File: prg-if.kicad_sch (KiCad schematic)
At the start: 30 parts, among them J201 PRG_USB, J202 MCU_RST, J203 MCU_BOOT0, J204 FT_TXD, J205 FT_RXD, J206 CONN_JTAG, Q201 MMBT3906, U201 FT2232HL, Y201 12MHz

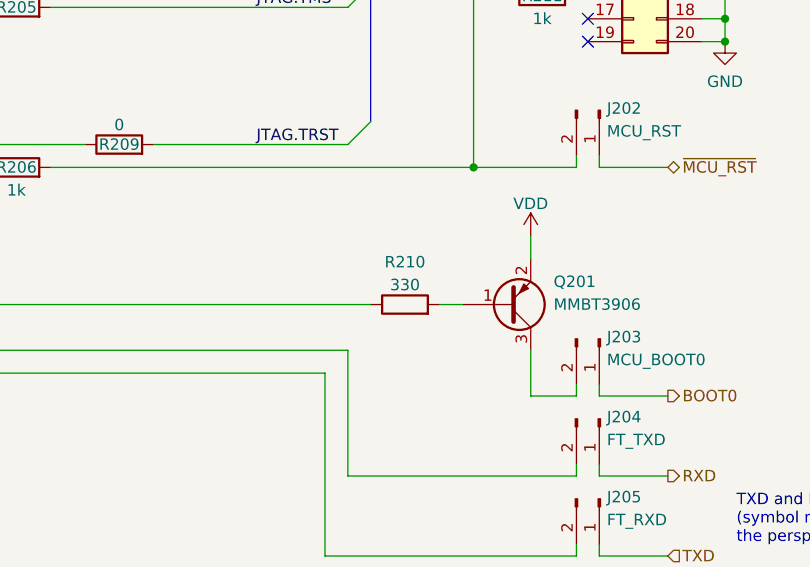
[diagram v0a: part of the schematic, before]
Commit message: Fix base resistor value
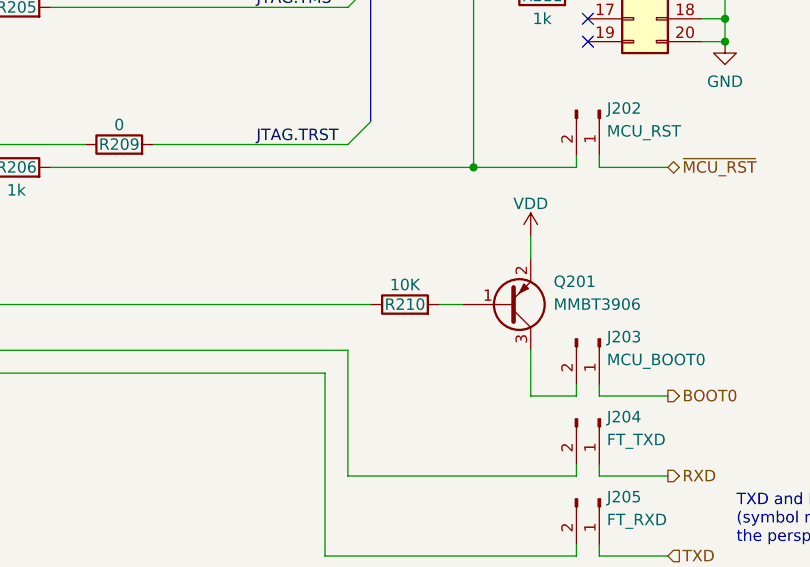
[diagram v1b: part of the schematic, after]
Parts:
- R210: value 330 -> 10K
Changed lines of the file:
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@@
   )
   (symbol (lib_id "Device:R") (at 214.63 106.68 90) (unit 1)
-    (in_bom yes) (on_board yes) (fields_autoplaced)
-    (property "Reference" "R210" (id 0) (at 214.63 101.9642 90))
-    (property "Value" "330" (id 1) (at 214.63 104.5011 90))
+    (in_bom yes) (on_board yes)
+    (property "Reference" "R210" (id 0) (at 214.63 106.68 90))
+    (property "Value" "10K" (id 1) (at 214.63 104.5011 90))
     (property "Footprint" "Resistor_SMD:R_0603_1608Metric_Pad0.98x0.95mm_HandSolder" (id 2) (at 214.63 108.458 90)
       (effects (font (size 1.27 1.27)) hide)

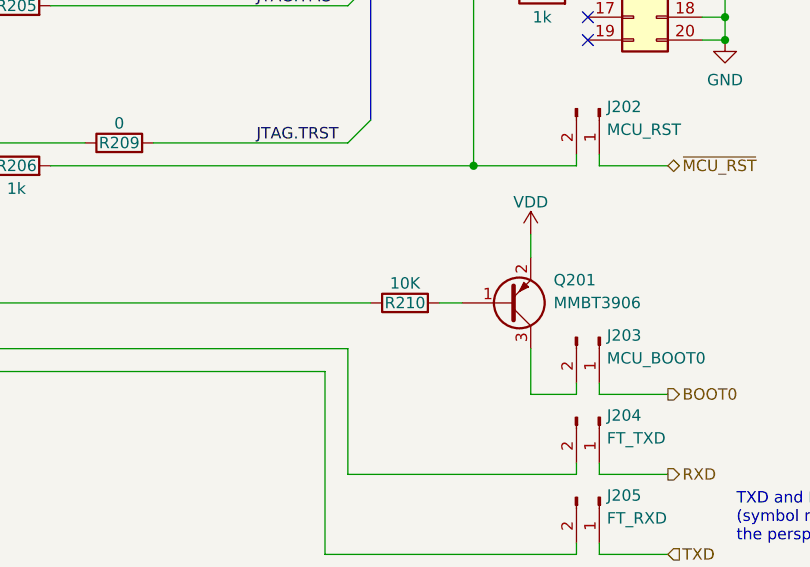
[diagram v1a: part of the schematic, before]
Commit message: Fully update PCB and schematic after BOM consolidation
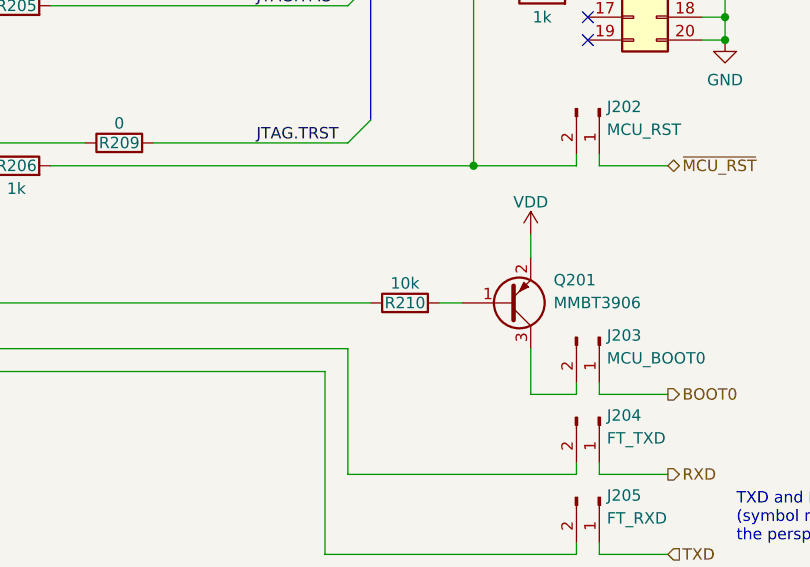
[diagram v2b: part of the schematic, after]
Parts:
- C201, C202: Part (none) -> 187-CL10C120JB81PNC
- C203, C206: Part 647-F920J475MPA -> 74-TMCP0J475MTRF
- C204, C205, C208: Part (none) -> 603-CC603ZRY5V7BB104
- C207: Part 963-LMK212B7335KG-T -> 810-C1608X7S0J335M0C
- FB201, FB202: Part 815-ACML-0603H-301 -> 603-PBY160808T-301YN
- J201: Part (none) -> 710-65100516121
- Q201: Part (none) -> 621-MMBT3906-F
- R201: Part (none) -> 652-CR0603FX-1202ELF
- R202, R206, R211: Part (none) -> 603-RC0603FR-071KL
- R203: Part (none) -> 791-RMC1/16-1002FTP
- R204, R205, R207, R208, R209: Part (none) -> 652-CR0603-J/-000ELF
- R210: value 10K -> 10k; Part (none) -> 791-RMC1/16-1002FTP
- U201: Part (none) -> 895-FT2232HL
- Y201: Part (none) -> 815-ABM3B-12-B2
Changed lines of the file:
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@@
+      (effects (font (size 1.27 1.27)) hide)
+    )
+    (property "Part" "603-CC603ZRY5V7BB104" (id 4) (at 83.82 53.34 0)
       (effects (font (size 1.27 1.27)) hide)
     )
@@
       (effects (font (size 1.27 1.27)) hide)
     )
-    (property "Part" "963-LMK212B7335KG-T" (id 4) (at 93.98 74.93 0)
+    (property "Part" "810-C1608X7S0J335M0C" (id 4) (at 93.98 74.93 0)
       (effects (font (size 1.27 1.27)) hide)
     )
@@
     )
     (property "Datasheet" "~" (id 3) (at 41.91 99.06 0)
+      (effects (font (size 1.27 1.27)) hide)
+    )
+    (property "Part" "710-65100516121" (id 4) (at 38.1 97.79 0)
       (effects (font (size 1.27 1.27)) hide)
     )
@@
       (effects (font (size 1.27 1.27)) hide)
     )
+    (property "Part" "652-CR0603FX-1202ELF" (id 4) (at 83.82 99.06 0)
+      (effects (font (size 1.27 1.27)) hide)
+    )
     (pin "1")
     (pin "2")
@@
       (effects (font (size 1.27 1.27)) hide)
     )
+    (property "Part" "652-CR0603-J/-000ELF" (id 4) (at 171.45 68.58 0)
+      (effects (font (size 1.27 1.27)) hide)
+    )
     (pin "1")
     (pin "2")
@@
       (effects (font (size 1.27 1.27)) hide)
     )
-    (property "Part" "647-F920J475MPA " (id 4) (at 73.66 53.34 0)
+    (property "Part" "74-TMCP0J475MTRF" (id 4) (at 73.66 53.34 0)
       (effects (font (size 1.27 1.27)) hide)
     )
@@
       (effects (font (size 1.27 1.27)) hide)
     )
+    (property "Part" "603-RC0603FR-071KL" (id 4) (at 92.71 104.14 0)
+      (effects (font (size 1.27 1.27)) hide)
+    )
     (pin "1")
     (pin "2")
@@
       (effects (font (size 1.27 1.27)) (justify left) hide)
     )
+    (property "Part" "621-MMBT3906-F" (id 4) (at 226.06 106.68 0)
+      (effects (font (size 1.27 1.27)) hide)
+    )
     (pin "1")
     (pin "2")
@@
     (in_bom yes) (on_board yes)
     (property "Reference" "R210" (id 0) (at 214.63 106.68 90))
-    (property "Value" "10K" (id 1) (at 214.63 104.5011 90))
+    (property "Value" "10k" (id 1) (at 214.63 104.5011 90))
     (property "Footprint" "Resistor_SMD:R_0603_1608Metric_Pad0.98x0.95mm_HandSolder" (id 2) (at 214.63 108.458 90)
       (effects (font (size 1.27 1.27)) hide)
     )
     (property "Datasheet" "~" (id 3) (at 214.63 106.68 0)
+      (effects (font (size 1.27 1.27)) hide)
+    )
+    (property "Part" "791-RMC1/16-1002FTP" (id 4) (at 214.63 106.68 0)
       (effects (font (size 1.27 1.27)) hide)
     )
@@
       (effects (font (size 1.27 1.27)) hide)
     )
+    (property "Part" "652-CR0603-J/-000ELF" (id 4) (at 181.61 66.04 0)
+      (effects (font (size 1.27 1.27)) hide)
+    )
     (pin "1")
     (pin "2")
@@
       (effects (font (size 1.27 1.27)) hide)
     )
-    (property "Part" "815-ACML-0603H-301" (id 4) (at 62.23 48.26 90)
+    (property "Part" "603-PBY160808T-301YN" (id 4) (at 62.23 48.26 90)
       (effects (font (size 1.27 1.27)) hide)
     )
@@
       (effects (font (size 1.27 1.27)) hide)
     )
+    (property "Part" "652-CR0603-J/-000ELF" (id 4) (at 181.61 71.12 0)
+      (effects (font (size 1.27 1.27)) hide)
+    )
     (pin "1")
     (pin "2")
@@
       (effects (font (size 1.27 1.27)) hide)
     )
+    (property "Part" "603-RC0603FR-071KL" (id 4) (at 171.45 91.44 0)
+      (effects (font (size 1.27 1.27)) hide)
+    )
     (pin "1")
     (pin "2")
@@
       (effects (font (size 1.27 1.27)) hide)
     )
-    (property "Part" "815-ACML-0603H-301" (id 4) (at 81.28 30.48 90)
+    (property "Part" "603-PBY160808T-301YN" (id 4) (at 81.28 30.48 90)
       (effects (font (size 1.27 1.27)) hide)
     )
@@
       (effects (font (size 1.27 1.27)) hide)
     )
+    (property "Part" "603-RC0603FR-071KL" (id 4) (at 229.87 72.39 0)
+      (effects (font (size 1.27 1.27)) hide)
+    )
     (pin "1")
     (pin "2")
@@
       (effects (font (size 1.27 1.27)) hide)
     )
+    (property "Part" "652-CR0603-J/-000ELF" (id 4) (at 182.88 88.9 0)
+      (effects (font (size 1.27 1.27)) hide)
+    )
     (pin "1")
     (pin "2")
@@
       (effects (font (size 1.27 1.27)) hide)
     )
+    (property "Part" "791-RMC1/16-1002FTP" (id 4) (at 92.71 137.16 0)
+      (effects (font (size 1.27 1.27)) hide)
+    )
     (pin "1")
     (pin "2")
@@
     )
     (property "Datasheet" "https://www.ftdichip.com/Support/Documents/DataSheets/ICs/DS_FT2232H.pdf" (id 3) (at 129.54 114.3 0)
+      (effects (font (size 1.27 1.27)) hide)
+    )
+    (property "Part" "895-FT2232HL" (id 4) (at 129.54 114.3 0)
       (effects (font (size 1.27 1.27)) hide)
     )
@@
       (effects (font (size 1.27 1.27)) hide)
     )
+    (property "Part" "603-CC603ZRY5V7BB104" (id 4) (at 82.55 74.93 0)
+      (effects (font (size 1.27 1.27)) hide)
+    )
     (pin "1")
     (pin "2")
@@
       (effects (font (size 1.27 1.27)) hide)
     )
-    (property "Part" "647-F920J475MPA " (id 4) (at 93.98 35.56 0)
+    (property "Part" "74-TMCP0J475MTRF" (id 4) (at 93.98 35.56 0)
       (effects (font (size 1.27 1.27)) hide)
     )
@@
     )
     (property "Datasheet" "~" (id 3) (at 171.45 73.66 0)
+      (effects (font (size 1.27 1.27)) hide)
+    )
+    (property "Part" "652-CR0603-J/-000ELF" (id 4) (at 171.45 73.66 0)
       (effects (font (size 1.27 1.27)) hide)
     )
@@
       (effects (font (size 1.27 1.27)) hide)
     )
+    (property "Part" "187-CL10C120JB81PNC" (id 4) (at 64.77 144.78 0)
+      (effects (font (size 1.27 1.27)) hide)
+    )
     (pin "1")
     (pin "2")
@@
       (effects (font (size 1.27 1.27)) hide)
     )
+    (property "Part" "815-ABM3B-12-B2" (id 4) (at 76.2 149.86 0)
+      (effects (font (size 1.27 1.27)) hide)
+    )
     (pin "1")
     (pin "2")
@@
     )
     (property "Datasheet" "~" (id 3) (at 104.14 35.56 0)
+      (effects (font (size 1.27 1.27)) hide)
+    )
+    (property "Part" "603-CC603ZRY5V7BB104" (id 4) (at 104.14 35.56 0)
       (effects (font (size 1.27 1.27)) hide)
     )
@@
       (effects (font (size 1.27 1.27)) hide)
     )
+    (property "Part" "187-CL10C120JB81PNC" (id 4) (at 64.77 154.94 0)
+      (effects (font (size 1.27 1.27)) hide)
+    )

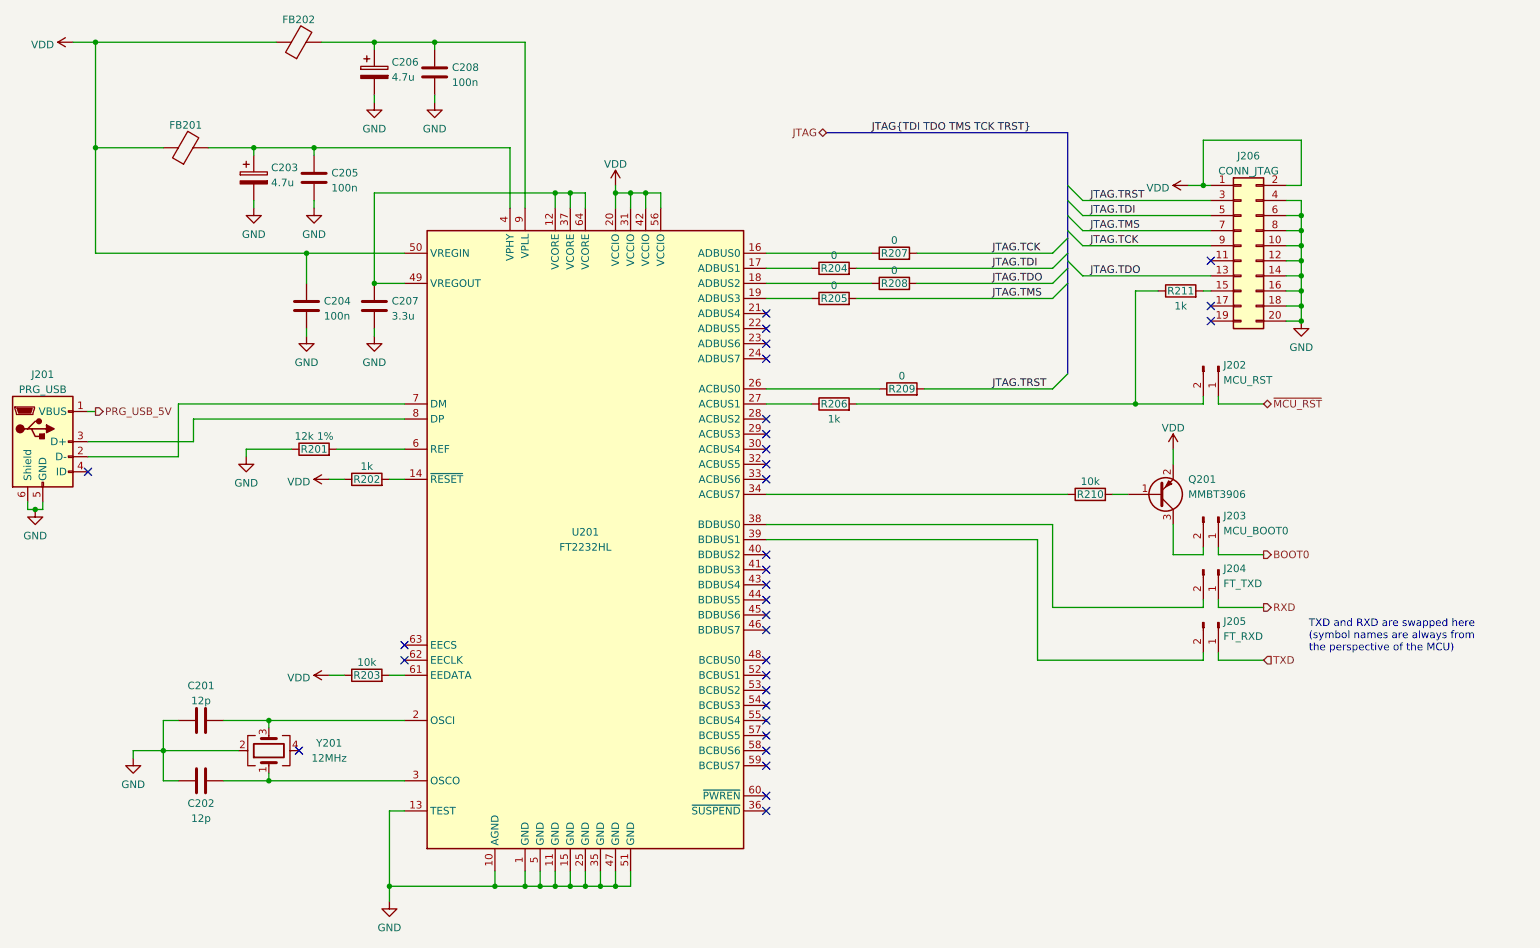
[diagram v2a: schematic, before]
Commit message: Move labels on switches, jumpers and so on to a separate Label property from the Value property.
Value must be the same for components that are physically the same, otherwise it screws up the BOM. But that means we need to add each label manually.
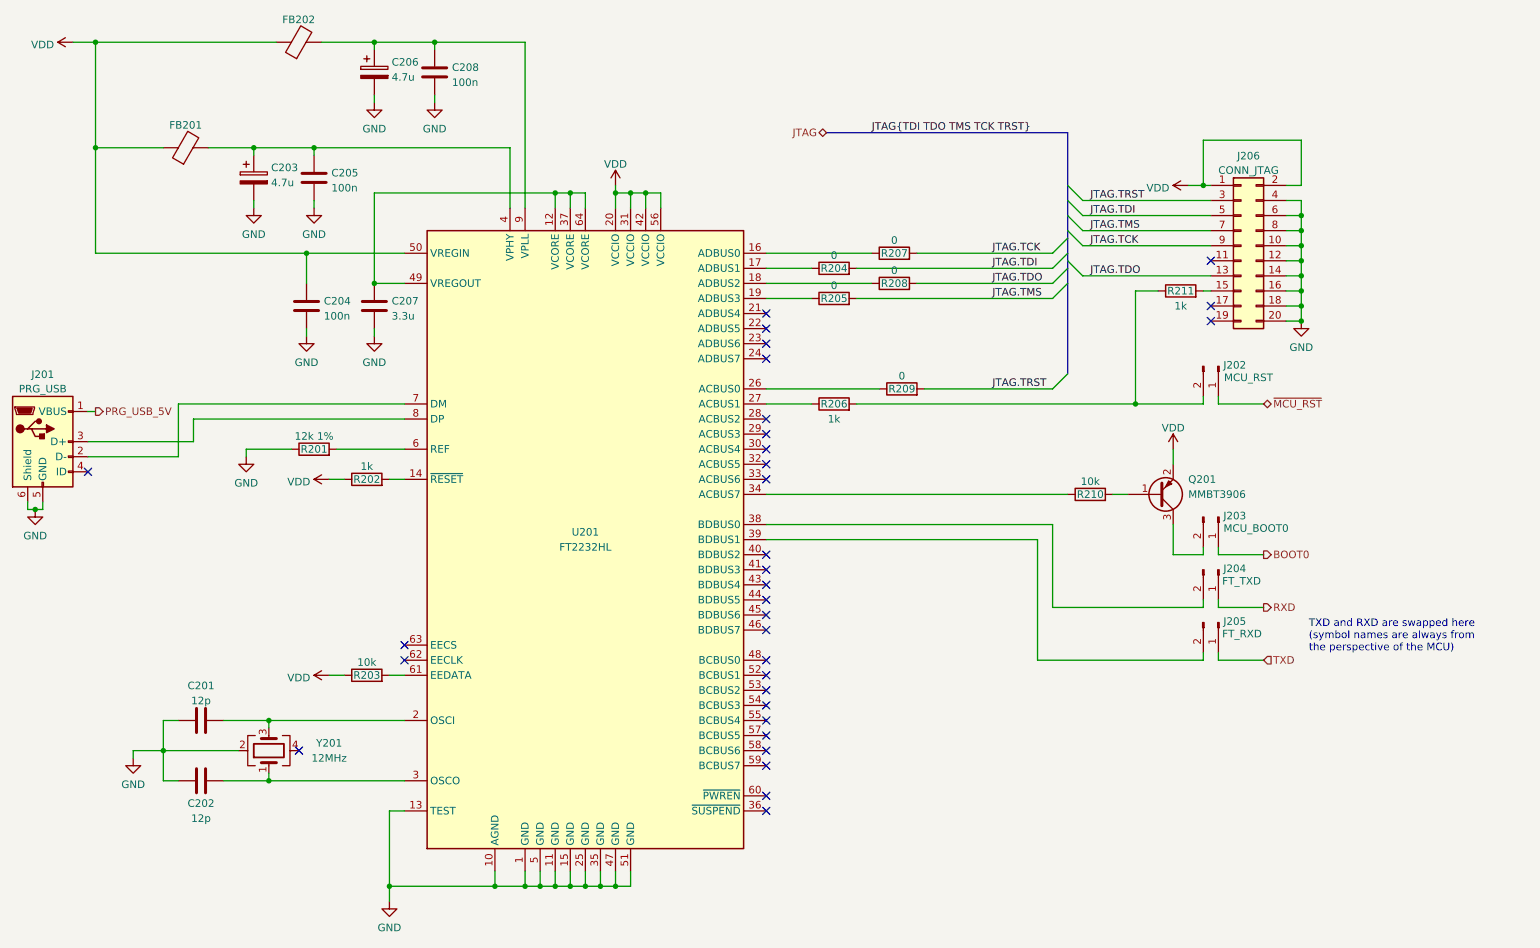
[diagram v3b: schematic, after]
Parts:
- J201: value PRG_USB -> USB_Mini-B; Label (none) -> PRG_USB
- J202: value MCU_RST -> PinHeader_2.54mm_1x02; Label (none) -> MCU_RST
- J203: value MCU_BOOT0 -> PinHeader_2.54mm_1x02; Label (none) -> MCU_BOOT0
- J204: value FT_TXD -> PinHeader_2.54mm_1x02; Label (none) -> FT_TXD
- J205: value FT_RXD -> PinHeader_2.54mm_1x02; Label (none) -> FT_RXD
- J206: value CONN_JTAG -> PinHeader_2.54mm_2x10; Label (none) -> CONN_JTAG
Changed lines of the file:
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@@
   )
   (symbol (lib_id "Connector:USB_B_Micro") (at 38.1 97.79 0) (unit 1)
-    (in_bom yes) (on_board yes) (fields_autoplaced)
+    (in_bom yes) (on_board yes)
     (property "Reference" "J201" (id 0) (at 38.1 86.4702 0))
-    (property "Value" "PRG_USB" (id 1) (at 38.1 89.0071 0))
+    (property "Value" "USB_Mini-B" (id 1) (at 38.1 89.0071 0)
+      (effects (font (size 1.27 1.27)) hide)
+    )
     (property "Footprint" "Connector_USB:USB_Mini-B_Wuerth_65100516121_Horizontal" (id 2) (at 41.91 99.06 0)
       (effects (font (size 1.27 1.27)) hide)
@@
       (effects (font (size 1.27 1.27)) hide)
     )
+    (property "Label" "PRG_USB" (id 5) (at 38.1 88.9 0))
     (pin "1")
     (pin "2")
@@
   )
   (symbol (lib_id "Connector:Conn_01x02_Male") (at 236.22 119.38 270) (unit 1)
-    (in_bom yes) (on_board yes) (fields_autoplaced)
+    (in_bom yes) (on_board yes)
     (property "Reference" "J204" (id 0) (at 237.0582 119.1803 90)
       (effects (font (size 1.27 1.27)) (justify left))
     )
-    (property "Value" "FT_TXD" (id 1) (at 237.0582 121.7172 90)
-      (effects (font (size 1.27 1.27)) (justify left))
+    (property "Value" "PinHeader_2.54mm_1x02" (id 1) (at 237.0582 121.7172 90)
+      (effects (font (size 1.27 1.27)) (justify left) hide)
     )
     (property "Footprint" "Connector_PinHeader_2.54mm:PinHeader_1x02_P2.54mm_Vertical" (id 2) (at 236.22 119.38 0)
@@
     (property "Datasheet" "~" (id 3) (at 236.22 119.38 0)
       (effects (font (size 1.27 1.27)) hide)
+    )
+    (property "Label" "FT_TXD" (id 4) (at 236.855 121.285 90)
+      (effects (font (size 1.27 1.27)) (justify left))
     )
     (pin "1")
@@
   )
   (symbol (lib_id "Connector:Conn_01x02_Male") (at 236.22 128.27 270) (unit 1)
-    (in_bom yes) (on_board yes) (fields_autoplaced)
+    (in_bom yes) (on_board yes)
     (property "Reference" "J205" (id 0) (at 237.0582 128.0703 90)
       (effects (font (size 1.27 1.27)) (justify left))
     )
-    (property "Value" "FT_RXD" (id 1) (at 237.0582 130.6072 90)
-      (effects (font (size 1.27 1.27)) (justify left))
+    (property "Value" "PinHeader_2.54mm_1x02" (id 1) (at 237.0582 130.6072 90)
+      (effects (font (size 1.27 1.27)) (justify left) hide)
     )
     (property "Footprint" "Connector_PinHeader_2.54mm:PinHeader_1x02_P2.54mm_Vertical" (id 2) (at 236.22 128.27 0)
@@
     (property "Datasheet" "~" (id 3) (at 236.22 128.27 0)
       (effects (font (size 1.27 1.27)) hide)
+    )
+    (property "Label" "FT_RXD" (id 4) (at 236.855 130.175 90)
+      (effects (font (size 1.27 1.27)) (justify left))
     )
     (pin "1")
@@
   )
   (symbol (lib_id "Connector_Generic:Conn_02x10_Odd_Even") (at 240.03 64.77 0) (unit 1)
-    (in_bom yes) (on_board yes) (fields_autoplaced)
+    (in_bom yes) (on_board yes)
     (property "Reference" "J206" (id 0) (at 241.3 49.6402 0))
-    (property "Value" "CONN_JTAG" (id 1) (at 241.3 52.1771 0))
+    (property "Value" "PinHeader_2.54mm_2x10" (id 1) (at 241.3 52.1771 0)
+      (effects (font (size 1.27 1.27)) hide)
+    )
     (property "Footprint" "Connector_PinSocket_2.54mm:PinSocket_2x10_P2.54mm_Vertical" (id 2) (at 240.03 64.77 0)
       (effects (font (size 1.27 1.27)) hide)
@@
       (effects (font (size 1.27 1.27)) hide)
     )
+    (property "Label" "CONN_JTAG" (id 4) (at 241.3 52.07 0))
     (pin "1")
     (pin "10")
@@
   )
   (symbol (lib_id "Connector:Conn_01x02_Male") (at 236.22 110.49 270) (unit 1)
-    (in_bom yes) (on_board yes) (fields_autoplaced)
+    (in_bom yes) (on_board yes)
     (property "Reference" "J203" (id 0) (at 237.0582 110.2903 90)
       (effects (font (size 1.27 1.27)) (justify left))
     )
-    (property "Value" "MCU_BOOT0" (id 1) (at 237.0582 112.8272 90)
-      (effects (font (size 1.27 1.27)) (justify left))
+    (property "Value" "PinHeader_2.54mm_1x02" (id 1) (at 237.0582 112.8272 90)
+      (effects (font (size 1.27 1.27)) (justify left) hide)
     )
     (property "Footprint" "Connector_PinHeader_2.54mm:PinHeader_1x02_P2.54mm_Vertical" (id 2) (at 236.22 110.49 0)
@@
       (effects (font (size 1.27 1.27)) hide)
     )
+    (property "Label" "MCU_BOOT0" (id 4) (at 242.57 112.395 90))
     (pin "1")
     (pin "2")
   )
   (symbol (lib_id "Connector:Conn_01x02_Male") (at 236.22 85.09 270) (unit 1)
-    (in_bom yes) (on_board yes) (fields_autoplaced)
+    (in_bom yes) (on_board yes)
     (property "Reference" "J202" (id 0) (at 237.0582 84.8903 90)
       (effects (font (size 1.27 1.27)) (justify left))
     )
-    (property "Value" "MCU_RST" (id 1) (at 237.0582 87.4272 90)
-      (effects (font (size 1.27 1.27)) (justify left))
+    (property "Value" "PinHeader_2.54mm_1x02" (id 1) (at 237.0582 87.4272 90)
+      (effects (font (size 1.27 1.27)) (justify left) hide)
     )
     (property "Footprint" "Connector_PinHeader_2.54mm:PinHeader_1x02_P2.54mm_Vertical" (id 2) (at 236.22 85.09 0)
@@
       (effects (font (size 1.27 1.27)) hide)
     )
-    (pin "1")
-    (pin "2")
+    (property "Label" "MCU_RST" (id 4) (at 241.3 86.995 90))
+    (pin "1")
+    (pin "2")
